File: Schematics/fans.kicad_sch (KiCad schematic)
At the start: 0 parts

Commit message: Motor Controllers
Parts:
- added C? (x2): 10uF, symbol Device:C_Small
- added J?: Fan 1, symbol Connector:Conn_01x02_Male
- added J?: Fan 2, symbol Connector:Conn_01x02_Male
- added U? (x2): LTC1695, symbol SFRLibraries:LTC1695
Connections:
- new net: J?.1 (Pin_1), U?.5 (Vout) (x2)
- new net +5V: C?.1, C?.1, U?.1 (VCC), U?.1 (VCC)
- new net Earth: C?.2, C?.2, J?.2 (Pin_2), J?.2 (Pin_2), U?.2 (GND), U?.2 (GND)
- new net SCL: U?.3 (SCL), U?.3 (SCL)
- new net SDA: U?.4 (SDA), U?.4 (SDA)

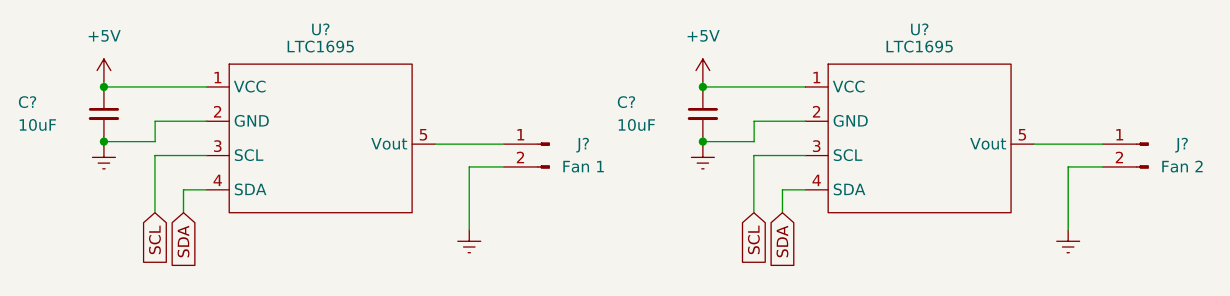
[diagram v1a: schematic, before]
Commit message: Changed MCU
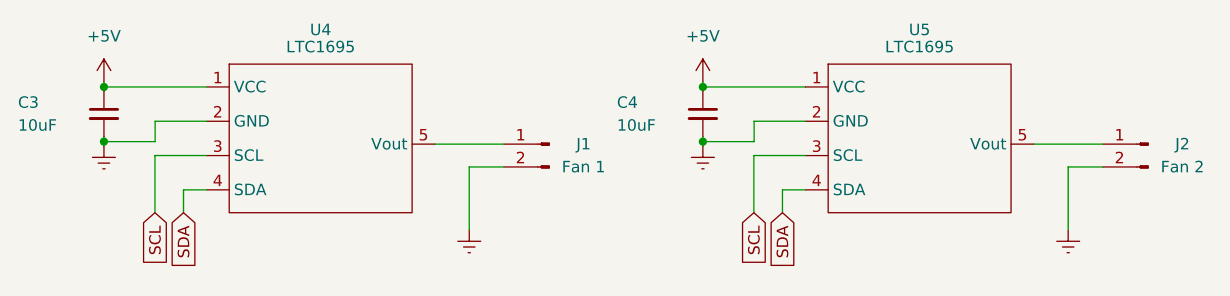
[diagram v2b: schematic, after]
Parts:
- gave numbers to parts that had none: 6
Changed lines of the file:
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@@
   (symbol (lib_id "SFRLibraries:LTC1695") (at 180.594 93.218 0) (unit 1)
     (in_bom yes) (on_board yes)
-    (property "Reference" "U?" (id 0) (at 180.594 86.868 0))
+    (property "Reference" "U5" (id 0) (at 180.594 86.868 0))
     (property "Value" "LTC1695" (id 1) (at 180.594 88.773 0))
     (property "Footprint" "" (id 2) (at 178.054 93.218 0)
@@
   (symbol (lib_id "power:Earth") (at 197.104 109.093 0) (unit 1)
     (in_bom yes) (on_board yes) (fields_autoplaced)
-    (property "Reference" "#PWR?" (id 0) (at 197.104 115.443 0)
+    (property "Reference" "#PWR028" (id 0) (at 197.104 115.443 0)
       (effects (font (size 1.27 1.27)) hide)
     )
@@
   (symbol (lib_id "Device:C_Small") (at 89.9668 96.2152 0) (unit 1)
     (in_bom yes) (on_board yes)
-    (property "Reference" "C?" (id 0) (at 80.4164 94.9452 0)
+    (property "Reference" "C3" (id 0) (at 80.4164 94.9452 0)
       (effects (font (size 1.27 1.27)) (justify left))
     )
@@
   (symbol (lib_id "power:Earth") (at 156.5148 99.7712 0) (unit 1)
     (in_bom yes) (on_board yes) (fields_autoplaced)
-    (property "Reference" "#PWR?" (id 0) (at 156.5148 106.1212 0)
+    (property "Reference" "#PWR026" (id 0) (at 156.5148 106.1212 0)
       (effects (font (size 1.27 1.27)) hide)
     )
@@
   (symbol (lib_id "Connector:Conn_01x02_Male") (at 139.446 99.568 0) (mirror y) (unit 1)
     (in_bom yes) (on_board yes)
-    (property "Reference" "J?" (id 0) (at 143.256 99.568 0))
+    (property "Reference" "J1" (id 0) (at 143.256 99.568 0))
     (property "Value" "Fan 1" (id 1) (at 143.256 102.108 0))
     (property "Footprint" "" (id 2) (at 139.446 99.568 0)
@@
   (symbol (lib_id "power:+5V") (at 156.5148 92.6592 0) (unit 1)
     (in_bom yes) (on_board yes) (fields_autoplaced)
-    (property "Reference" "#PWR?" (id 0) (at 156.5148 96.4692 0)
+    (property "Reference" "#PWR024" (id 0) (at 156.5148 96.4692 0)
       (effects (font (size 1.27 1.27)) hide)
     )
@@
   (symbol (lib_id "Device:C_Small") (at 156.5148 96.2152 0) (unit 1)
     (in_bom yes) (on_board yes)
-    (property "Reference" "C?" (id 0) (at 146.9644 94.9452 0)
+    (property "Reference" "C4" (id 0) (at 146.9644 94.9452 0)
       (effects (font (size 1.27 1.27)) (justify left))
     )
@@
   (symbol (lib_id "power:Earth") (at 89.9668 99.7712 0) (unit 1)
     (in_bom yes) (on_board yes) (fields_autoplaced)
-    (property "Reference" "#PWR?" (id 0) (at 89.9668 106.1212 0)
+    (property "Reference" "#PWR025" (id 0) (at 89.9668 106.1212 0)
       (effects (font (size 1.27 1.27)) hide)
     )
@@
   (symbol (lib_id "power:+5V") (at 89.9668 92.6592 0) (unit 1)
     (in_bom yes) (on_board yes) (fields_autoplaced)
-    (property "Reference" "#PWR?" (id 0) (at 89.9668 96.4692 0)
+    (property "Reference" "#PWR023" (id 0) (at 89.9668 96.4692 0)
       (effects (font (size 1.27 1.27)) hide)
     )
@@
   (symbol (lib_id "power:Earth") (at 130.556 109.093 0) (unit 1)
     (in_bom yes) (on_board yes) (fields_autoplaced)
-    (property "Reference" "#PWR?" (id 0) (at 130.556 115.443 0)
+    (property "Reference" "#PWR027" (id 0) (at 130.556 115.443 0)
       (effects (font (size 1.27 1.27)) hide)
     )
@@
   (symbol (lib_id "SFRLibraries:LTC1695") (at 114.046 93.218 0) (unit 1)
     (in_bom yes) (on_board yes)
-    (property "Reference" "U?" (id 0) (at 114.046 86.868 0))
+    (property "Reference" "U4" (id 0) (at 114.046 86.868 0))
     (property "Value" "LTC1695" (id 1) (at 114.046 88.773 0))
     (property "Footprint" "" (id 2) (at 111.506 93.218 0)
@@
   (symbol (lib_id "Connector:Conn_01x02_Male") (at 205.994 99.568 0) (mirror y) (unit 1)
     (in_bom yes) (on_board yes)
-    (property "Reference" "J?" (id 0) (at 209.804 99.568 0))
+    (property "Reference" "J2" (id 0) (at 209.804 99.568 0))
     (property "Value" "Fan 2" (id 1) (at 209.804 102.108 0))
     (property "Footprint" "" (id 2) (at 205.994 99.568 0)

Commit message: Added Footprints
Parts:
- C3, C4: footprint (none) -> Resistor_SMD:R_0603_1608Metric_Pad0.98x0.95mm_HandSolder
- J1, J2: footprint (none) -> SFRFootprints:Fan
- U4, U5: footprint (none) -> SFRFootprints:LTC1695CS5-TRPBF
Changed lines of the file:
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@@
     (property "Reference" "U5" (id 0) (at 180.594 86.868 0))
     (property "Value" "LTC1695" (id 1) (at 180.594 88.773 0))
-    (property "Footprint" "" (id 2) (at 178.054 93.218 0)
+    (property "Footprint" "SFRFootprints:LTC1695CS5-TRPBF" (id 2) (at 178.054 93.218 0)
       (effects (font (size 1.27 1.27)) hide)
     )
@@
       (effects (font (size 1.27 1.27)) (justify left))
     )
-    (property "Footprint" "" (id 2) (at 89.9668 96.2152 0)
+    (property "Footprint" "Resistor_SMD:R_0603_1608Metric_Pad0.98x0.95mm_HandSolder" (id 2) (at 89.9668 96.2152 0)
       (effects (font (size 1.27 1.27)) hide)
     )
@@
     (property "Reference" "J1" (id 0) (at 143.256 99.568 0))
     (property "Value" "Fan 1" (id 1) (at 143.256 102.108 0))
-    (property "Footprint" "" (id 2) (at 139.446 99.568 0)
+    (property "Footprint" "SFRFootprints:Fan" (id 2) (at 139.446 99.568 0)
       (effects (font (size 1.27 1.27)) hide)
     )
@@
       (effects (font (size 1.27 1.27)) (justify left))
     )
-    (property "Footprint" "" (id 2) (at 156.5148 96.2152 0)
+    (property "Footprint" "Resistor_SMD:R_0603_1608Metric_Pad0.98x0.95mm_HandSolder" (id 2) (at 156.5148 96.2152 0)
       (effects (font (size 1.27 1.27)) hide)
     )
@@
     (property "Reference" "U4" (id 0) (at 114.046 86.868 0))
     (property "Value" "LTC1695" (id 1) (at 114.046 88.773 0))
-    (property "Footprint" "" (id 2) (at 111.506 93.218 0)
+    (property "Footprint" "SFRFootprints:LTC1695CS5-TRPBF" (id 2) (at 111.506 93.218 0)
       (effects (font (size 1.27 1.27)) hide)
     )
@@
     (property "Reference" "J2" (id 0) (at 209.804 99.568 0))
     (property "Value" "Fan 2" (id 1) (at 209.804 102.108 0))
-    (property "Footprint" "" (id 2) (at 205.994 99.568 0)
+    (property "Footprint" "SFRFootprints:Fan" (id 2) (at 205.994 99.568 0)
       (effects (font (size 1.27 1.27)) hide)
     )
